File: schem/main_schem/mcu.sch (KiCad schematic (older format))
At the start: 31 parts, among them P1 CONN_ICD, SW1 SW_RESET, U1 25LC256, U2 PIC18F97J60, X1 25MHz

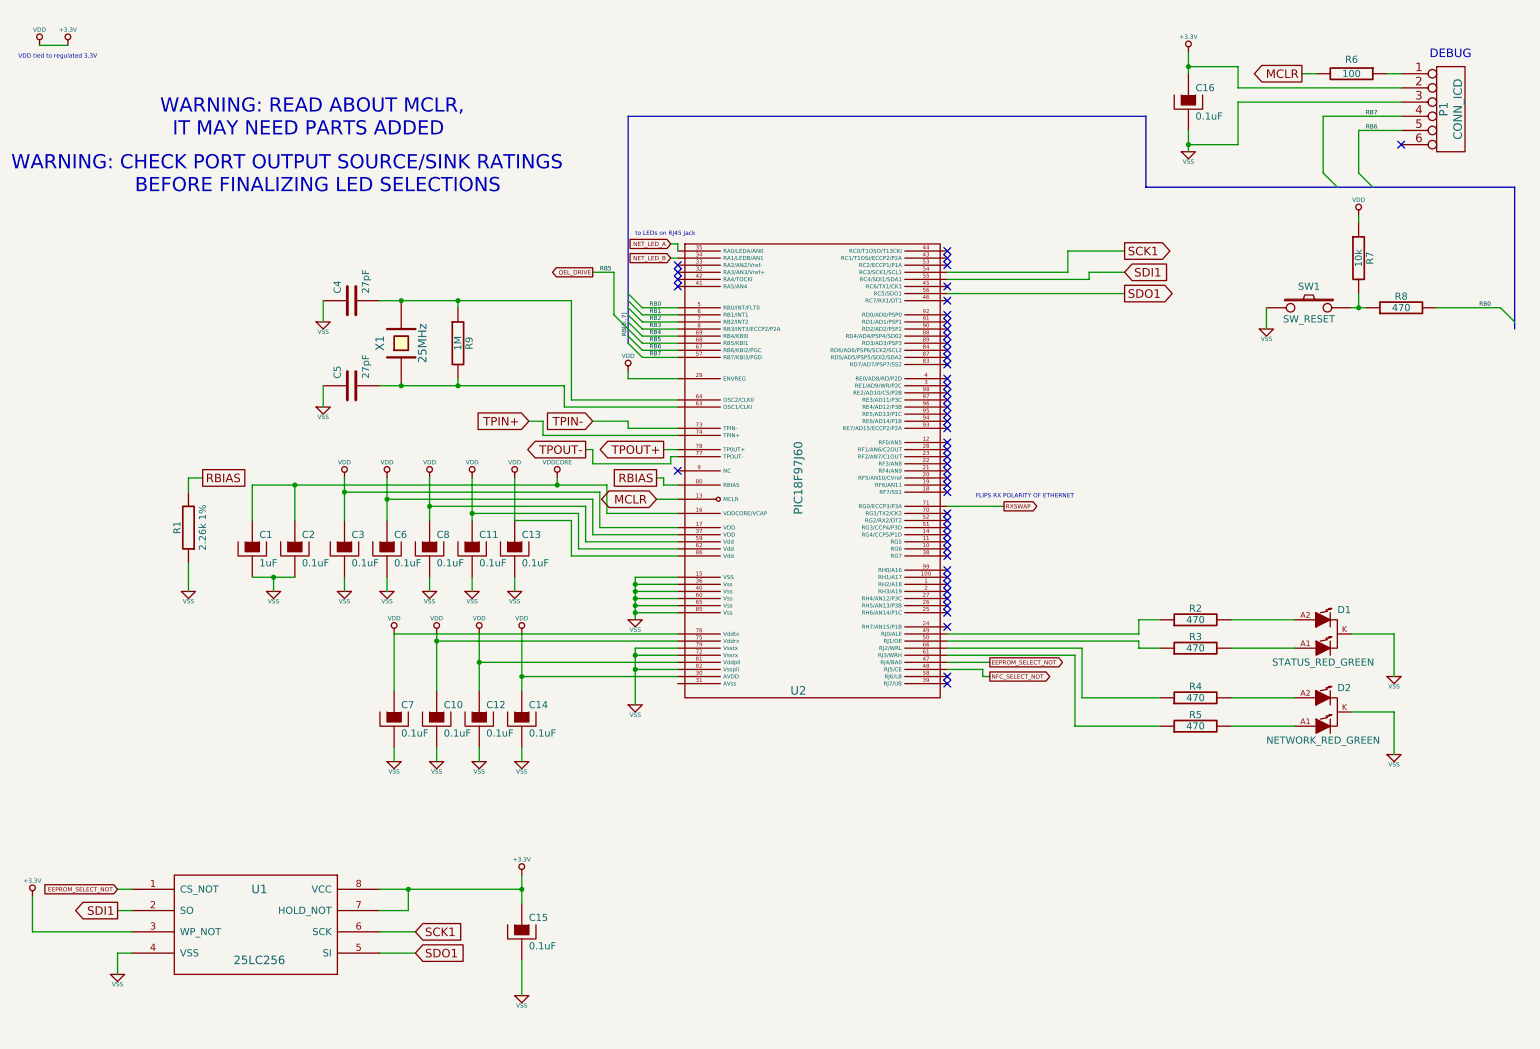
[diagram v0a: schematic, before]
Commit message: Begin board, layout mcu, xtal, eeprom
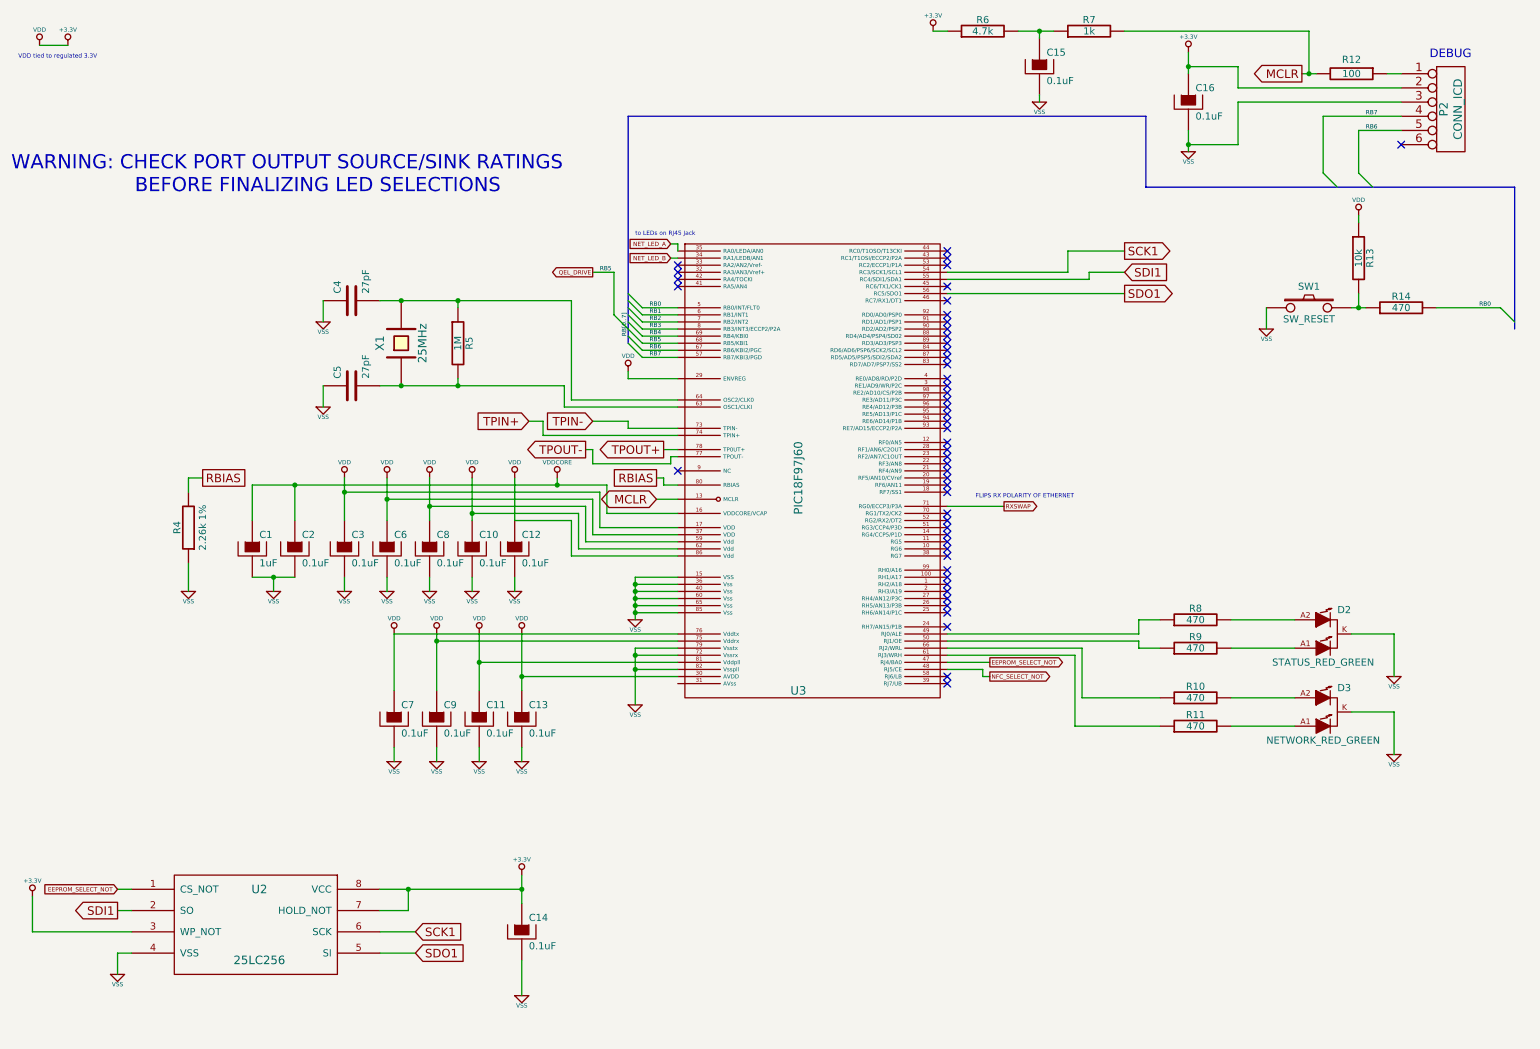
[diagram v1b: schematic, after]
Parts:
- added C15: 0.1uF, symbol CP
- added R6: 4.7k, symbol R
- added R7: 1k, symbol R
- renumbered C11 to C10, C12 to C11, C13 to C12, C14 to C13, C15 to C14, C10 to C9, D1 to D2, D2 to D3, P1 to P2, R4 to R10, R5 to R11, R6 to R12, R7 to R13, R8 to R14, R1 to R4, R9 to R5, R2 to R8, R3 to R9, U1 to U2, U2 to U3
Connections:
- net +3.3V: now also R6.1
- net MCLR: now also R7.2
- net VSS: now also C15.2
- new net: C15.1, R6.2, R7.1
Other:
- note removed: "WARNING: READ ABOUT MCLR,\n IT MAY NEED PARTS ADDED"

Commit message: Ethernet Anolog, breakout pins, SPI iface breakout for NFC
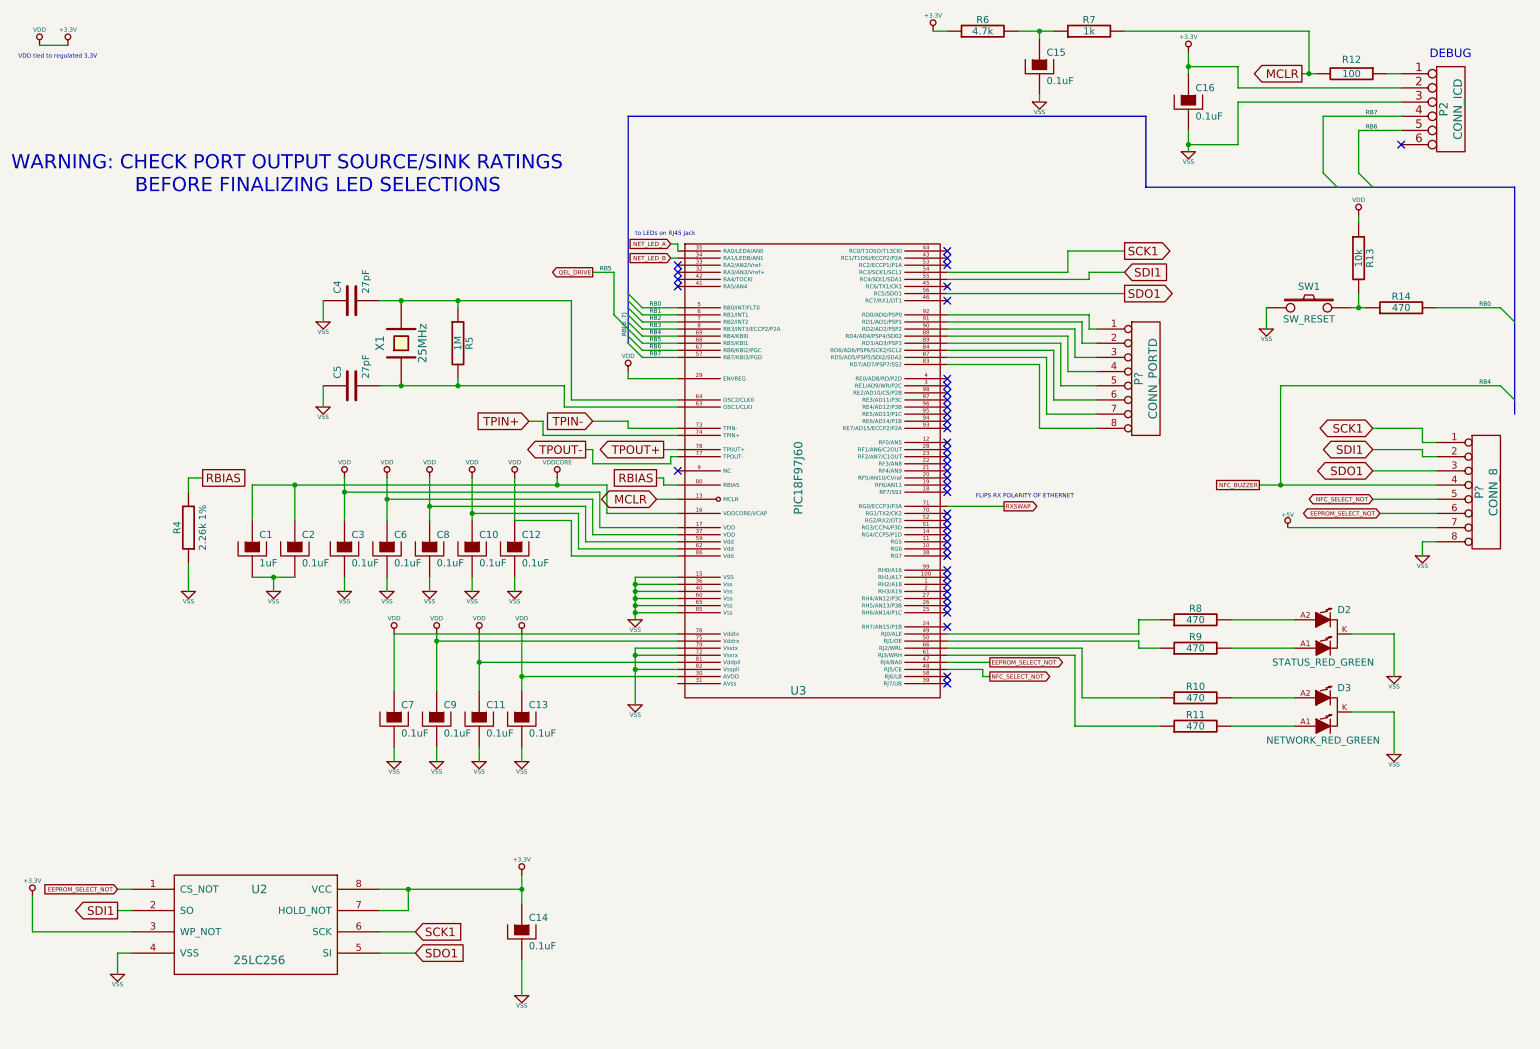
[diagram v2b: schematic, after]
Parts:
- added P?: CONN_PORTD, symbol CONN_8
- added P?: CONN_8, symbol CONN_8
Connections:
- net EEPROM_SELECT_NOT: now also P?.6 (P6)
- net NFC_SELECT_NOT: now also P?.5 (P5)
- net SCK1: now also P?.1 (P1)
- net SDI1: now also P?.2 (P2)
- net SDO1: now also P?.3 (P3)
- net VSS: now also P?.8 (P8)
- net at U3.83 (RD7/AD7/PSP7/SS2): now also P?.8 (P8)
- net at U3.84 (RD6/AD6/PSP6/SCK2/SCL2): now also P?.6 (P6)
- net at U3.87 (RD5/AD5/PSP5/SDI2/SDA2): now also P?.7 (P7)
- net at U3.88 (RD4/AD4/PSP4/SD02): now also P?.4 (P4)
- net at U3.89 (RD3/AD3/PSP3): now also P?.5 (P5)
- net at U3.90 (RD2/AD2/PSP2): now also P?.3 (P3)
- net at U3.91 (RD1/AD1/PSP1): now also P?.2 (P2)
- net at U3.92 (RD0/AD0/PSP0): now also P?.1 (P1)
- net RB4 renamed NFC_BUZZER
- net NFC_BUZZER: now also P?.4 (P4)
- new net +5V: P?.7 (P7)
- no-connect marks 52 -> 44

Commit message: BOM sheets, update ethernet analog circuit
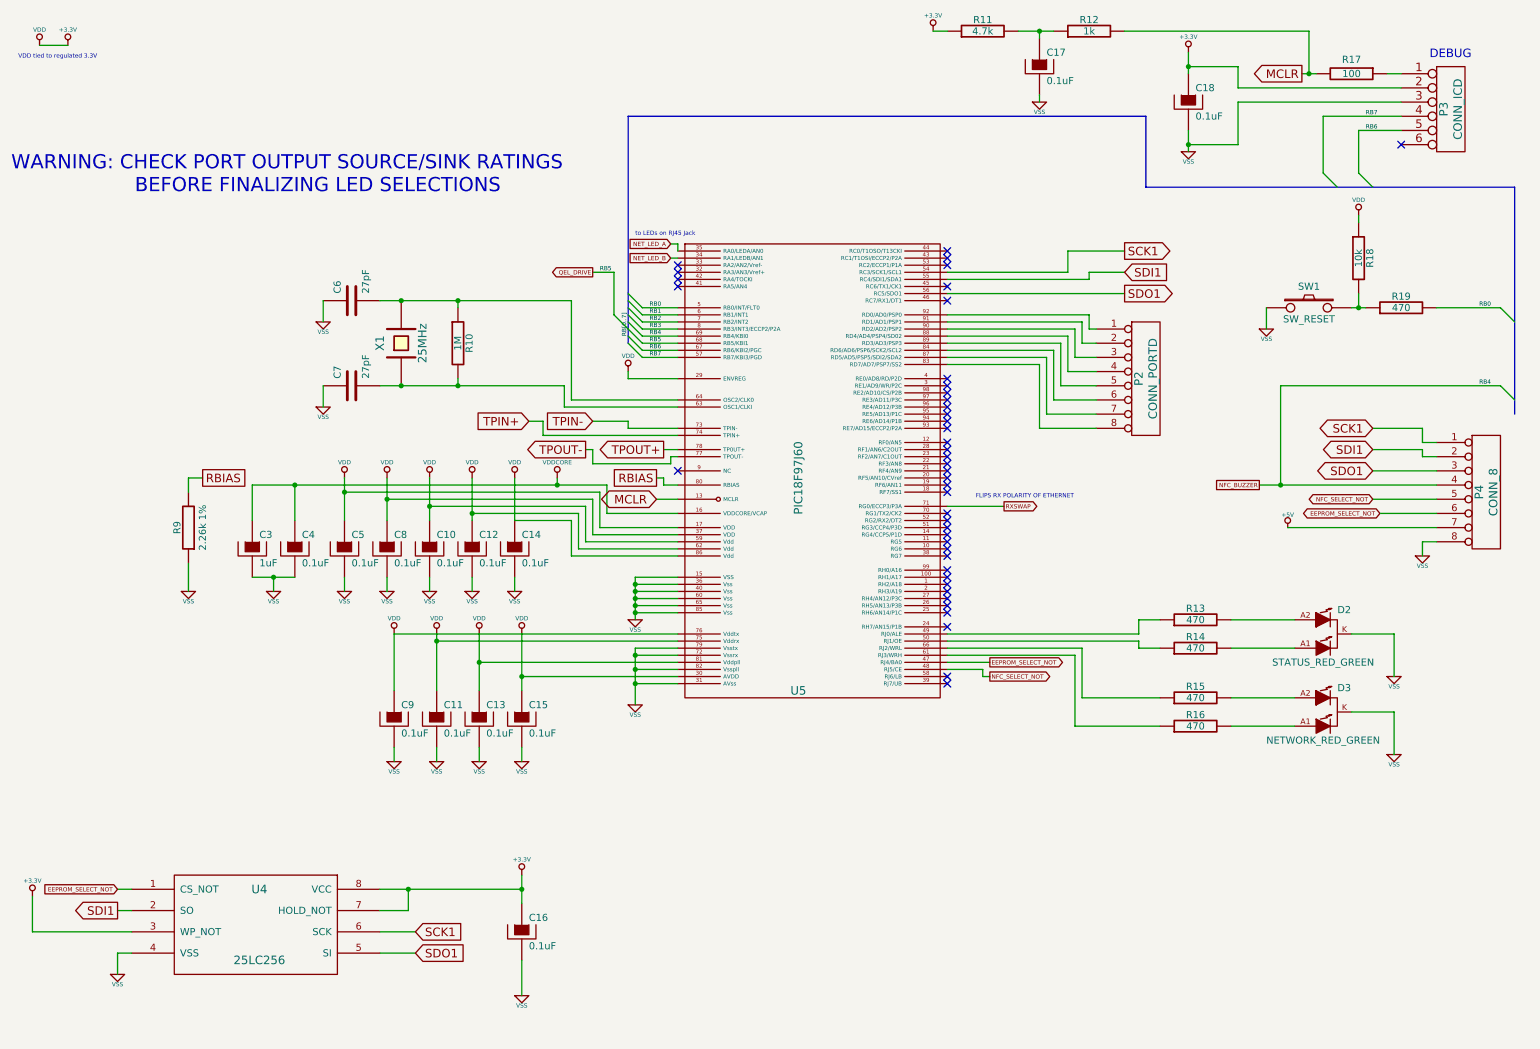
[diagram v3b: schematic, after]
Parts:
- gave numbers to parts that had none: 2
- renumbered C8 to C10, C9 to C11, C10 to C12, C11 to C13, C12 to C14, C13 to C15, C14 to C16, C15 to C17, C16 to C18, C1 to C3, C2 to C4, C3 to C5, C4 to C6, C5 to C7, C6 to C8, C7 to C9, P2 to P3, R5 to R10, R6 to R11, R7 to R12, R8 to R13, R9 to R14, R10 to R15, R11 to R16, R12 to R17, R13 to R18, R14 to R19, R4 to R9, U2 to U4, U3 to U5
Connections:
- net VSS: now also U5.31 (AVss)

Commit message: Cleanup MCU portion, add NFC buzzer breakout and driver
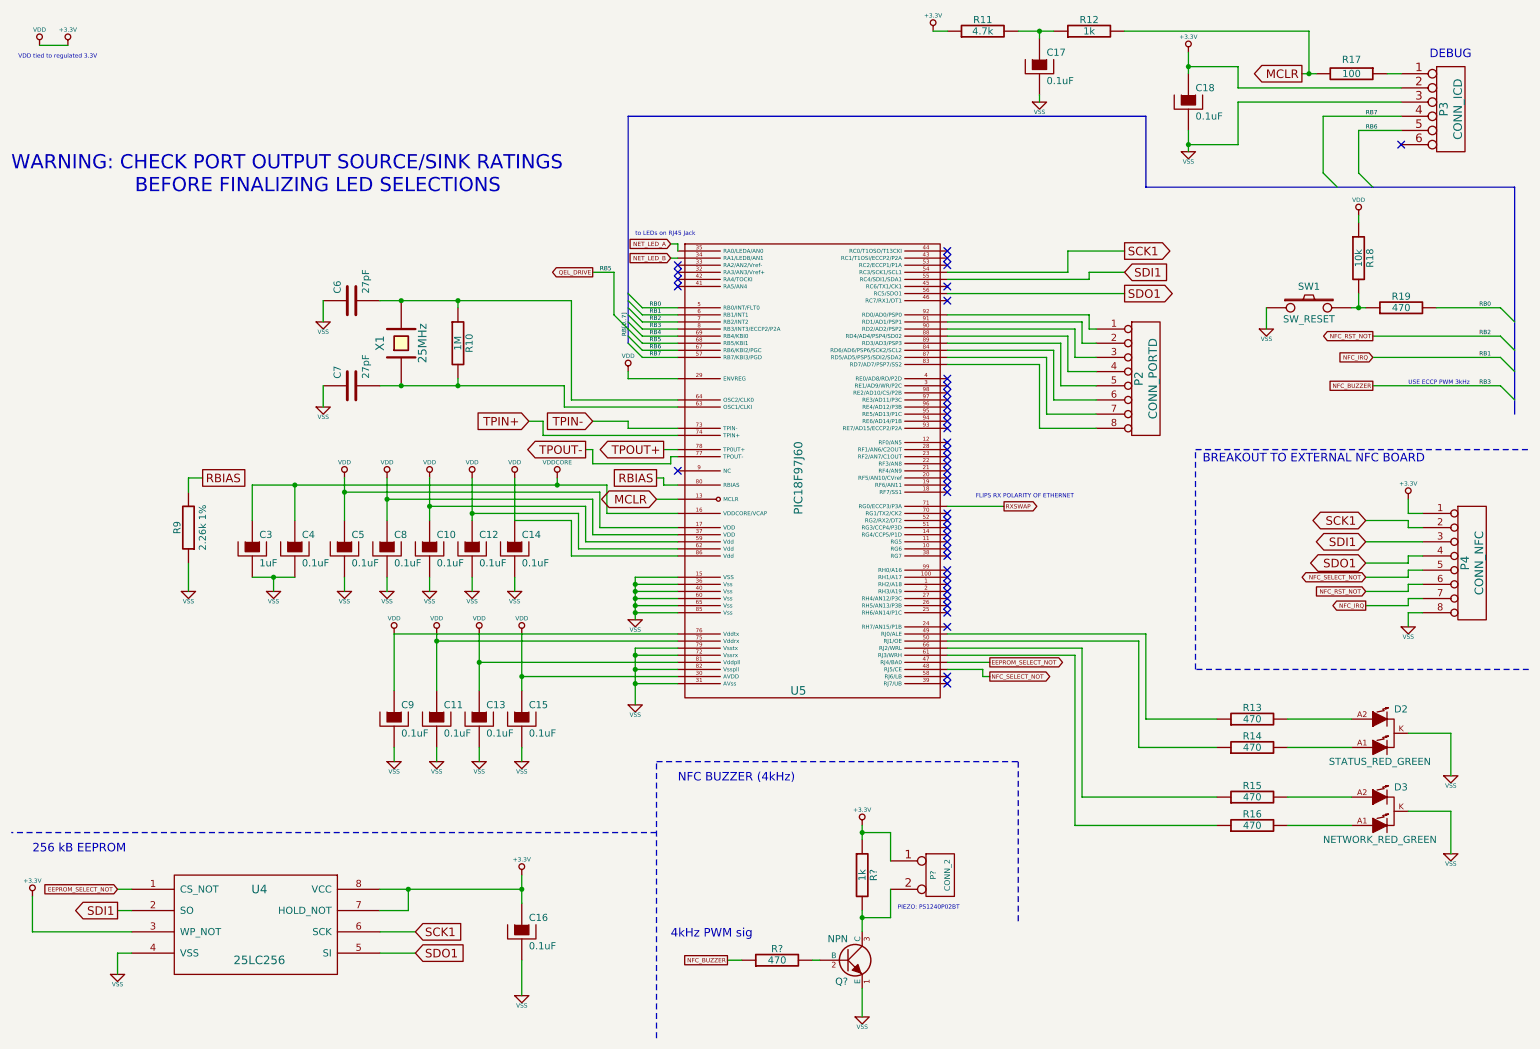
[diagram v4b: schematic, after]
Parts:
- added P?: CONN_2, symbol CONN_2
- added Q?: NPN, symbol NPN
- added R?: 470, symbol R
- added R?: 1k, symbol R
- P4: value CONN_8 -> CONN_NFC
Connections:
- net RB1 is gone; now on net NFC_IRQ: U5.6 (RB1/INT1)
- net RB3 is gone; now on net NFC_BUZZER: U5.8 (RB3/INT3/ECCP2/P2A)
- net +3.3V: now also P4.1 (P1), P?.1 (P1), R?.1
- net EEPROM_SELECT_NOT: no longer P4.6 (P6)
- net NFC_BUZZER: now also R?.1; no longer P4.4 (P4), U5.69 (RB4/KBI0)
- net SCK1: now also P4.2 (P2); no longer P4.1 (P1)
- net SDI1: now also P4.3 (P3); no longer P4.2 (P2)
- net SDO1: now also P4.4 (P4); no longer P4.3 (P3)
- net VSS: now also Q?.1 (E)
- net +5V renamed NFC_IRQ
- net RB2 renamed NFC_RST_NOT
- net NFC_RST_NOT: now also P4.6 (P6)
- new net: Q?.2 (B), R?.2
- new net: P?.2 (PM), Q?.3 (C), R?.2
- new net RB4: U5.69 (RB4/KBI0)
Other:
- note added: "256 kB EEPROM"
- note added: "4kHz PWM sig"
- note added: "BREAKOUT TO EXTERNAL NFC BOARD"
- note added: "NFC BUZZER (4kHz)"
- note added: "PIEZO: PS1240P02BT"
- note added: "USE ECCP PWM 3kHz"
- moved on the sheet: D2, D3, P4, R13, R14, R15, R16

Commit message: Complete BOM
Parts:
- R13, R14, R15, R16: value 470 -> 220
- gave numbers to parts that had none: 4
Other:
- note added: "for XC1671CT-ND:\n c_l = 18pF\n\nC7=C8=Cb\n\nCb / 2 + (2 to 5 pF) = cl\n27/2 + 3.5 = 17pF --> about 18 pF"
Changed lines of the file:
@@
-EESchema Schematic File Version 2  date 10/7/2012 9:06:12 PM
+EESchema Schematic File Version 2  date 10/8/2012 12:57:14 PM
 LIBS:power
 LIBS:device
@@
 Comment4 ""
 $EndDescr
+Text Notes 2000 2650 0    30   ~ 0
+for XC1671CT-ND:\n c_l = 18pF\n\nC7=C8=Cb\n\nCb / 2 + (2 to 5 pF) = cl\n27/2 + 3.5 = 17pF --> about 18 pF
 Text Notes 8900 3700 0    60   ~ 0
 BREAKOUT TO EXTERNAL NFC BOARD
@@
 PIEZO: PS1240P02BT
 $Comp
-L CONN_2 P?
+L CONN_2 P5
 U 1 1 50703F74
 P 7050 6600
-F 0 "P?" V 7000 6600 40  0000 C CNN
+F 0 "P5" V 7000 6600 40  0000 C CNN
 F 1 "CONN_2" V 7100 6600 40  0000 C CNN
 	1    7050 6600
@@
 $EndComp
 $Comp
-L R R?
+L R R20
 U 1 1 50703F34
 P 6500 6600
-F 0 "R?" V 6580 6600 50  0000 C CNN
+F 0 "R20" V 6580 6600 50  0000 C CNN
 F 1 "1k" V 6500 6600 50  0000 C CNN
 	1    6500 6600
@@
 $EndComp
 $Comp
-L R R?
+L R R19
 U 1 1 50703DAF
 P 5900 7200
-F 0 "R?" V 5980 7200 50  0000 C CNN
+F 0 "R19" V 5980 7200 50  0000 C CNN
 F 1 "470" V 5900 7200 50  0000 C CNN
 	1    5900 7200
@@
 NFC_BUZZER
 $Comp
-L NPN Q?
+L NPN Q2
 U 1 1 50703D8E
 P 6400 7200
-F 0 "Q?" H 6400 7050 50  0000 R CNN
+F 0 "Q2" H 6400 7050 50  0000 R CNN
 F 1 "NPN" H 6400 7350 50  0000 R CNN
 	1    6400 7200
@@
 P 9250 6250
 F 0 "R16" V 9330 6250 50  0000 C CNN
-F 1 "470" V 9250 6250 50  0000 C CNN
+F 1 "220" V 9250 6250 50  0000 C CNN
 	1    9250 6250
 	0    -1   -1   0
@@
 P 9250 6050
 F 0 "R15" V 9330 6050 50  0000 C CNN
-F 1 "470" V 9250 6050 50  0000 C CNN
+F 1 "220" V 9250 6050 50  0000 C CNN
 	1    9250 6050
 	0    -1   -1   0
@@
 P 9250 5700
 F 0 "R14" V 9330 5700 50  0000 C CNN
-F 1 "470" V 9250 5700 50  0000 C CNN
+F 1 "220" V 9250 5700 50  0000 C CNN
 	1    9250 5700
 	0    -1   -1   0
@@
 P 9250 5500
 F 0 "R13" V 9330 5500 50  0000 C CNN
-F 1 "470" V 9250 5500 50  0000 C CNN
+F 1 "220" V 9250 5500 50  0000 C CNN
 	1    9250 5500
 	0    -1   -1   0
